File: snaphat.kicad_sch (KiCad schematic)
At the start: 140 parts, among them J1 Conn_01x08_S8B-PH-K-S(LF)(SN), J2 Conn_02x20_2214SM-40G-75-PCR, J3 Conn_01x02_B2B-PH-K-S(LF)(SN), J4 USB_C_USB4125-GF-A-0190, J5 Conn_01x03_MC34747, Q1 Q_BC817-25, Q2 Q_NTR4003NT1G, Q3 Q_NTR4003NT1G, SW1 SW_B3FS-1050, SW2 SW_B3FS-1050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

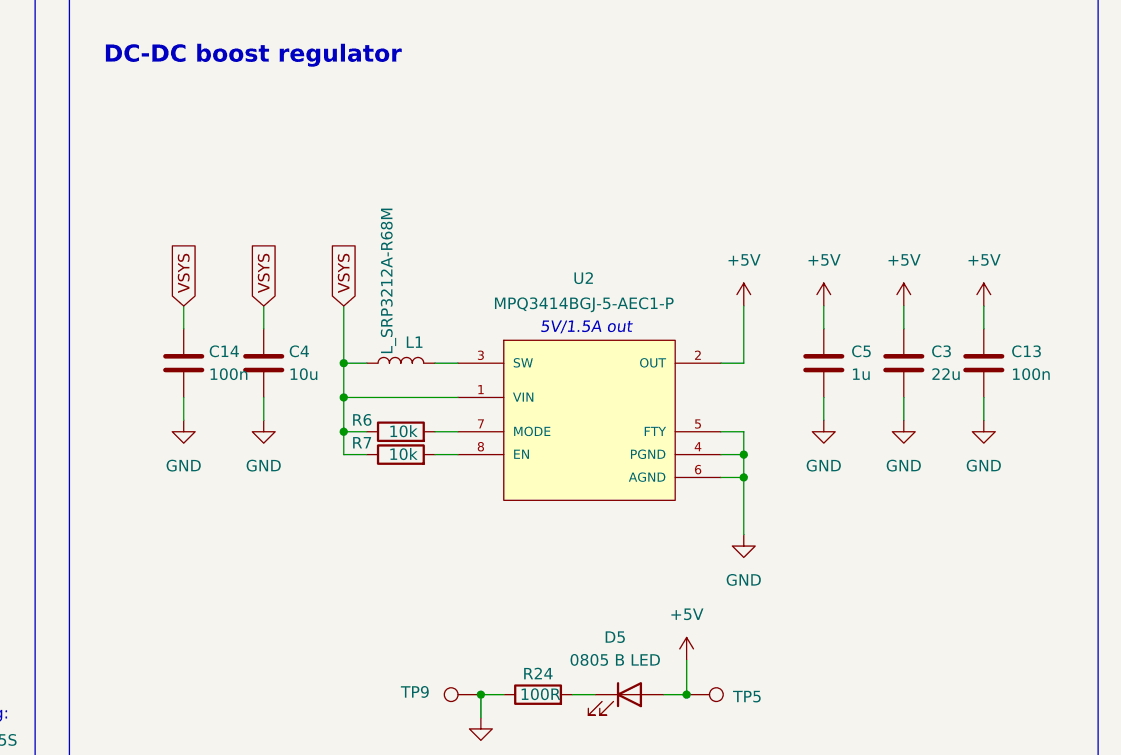
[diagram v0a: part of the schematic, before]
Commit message: Replace boost regulator with MIC2250-1YD5-TR
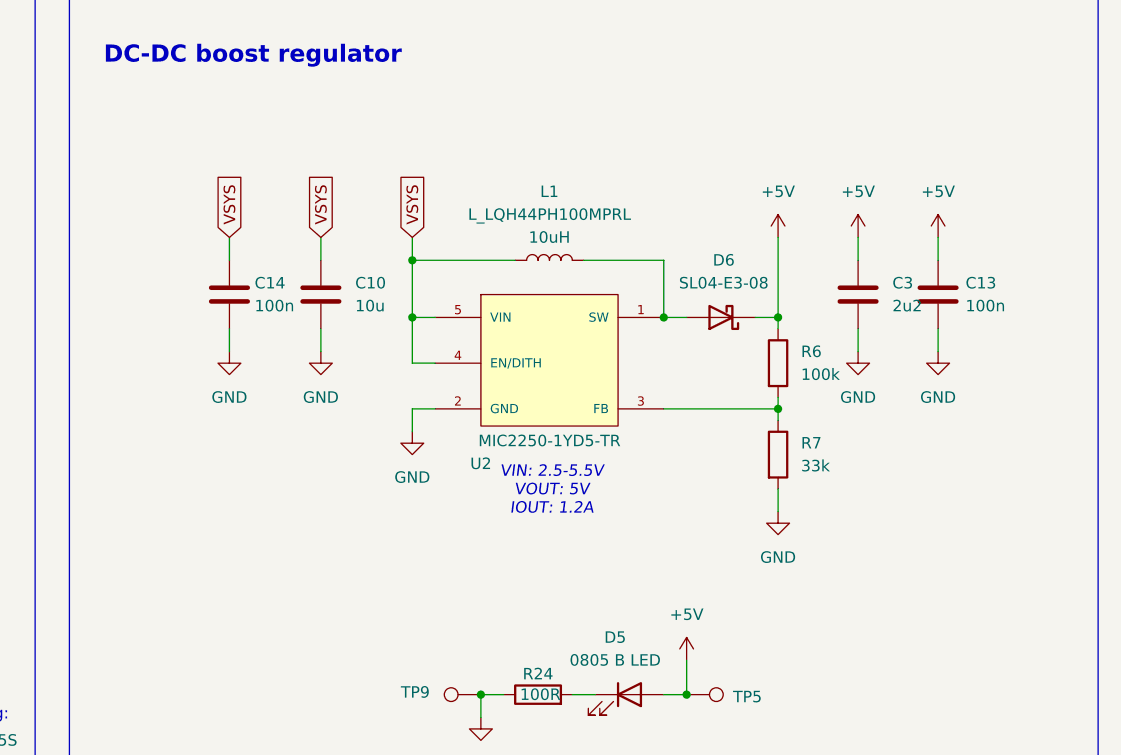
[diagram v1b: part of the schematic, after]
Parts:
- removed C3: 22u, library:C_0805_2012Metric, symbol library:C_22u_0805
- removed C4: 10u, library:C_0805_2012Metric, symbol library:C_10u_0805
- removed C5: 1u, library:C_0805_2012Metric, symbol library:C_1u_0805
- removed L1: L_SRP3212A-R68M, library:L_1210_3225Metric, symbol library:L_SRP3212A-R68M
- removed R6, R7: 10k, library:R_0402_1005Metric, symbol library:R_10k_0402
- removed U2: MPQ3414BGJ-5-AEC1-P, library:TSOT-23-8, symbol library:MPQ3414BGJ-5-AEC1-P
- added C10: 10u, library:C_0805_2012Metric, symbol library:C_10u_0805
- added C3: 2u2, library:C_0805_2012Metric, symbol library:C_2u2_0805
- added D6: SL04-E3-08, library:DO-219AB, symbol library:D_SL04-E3-08
- added L1: L_LQH44PH100MPRL, library:L_LPH44PH, symbol library:L_LQH44PH100MPRL
- added R6: 100k, library:R_0402_1005Metric, symbol library:R_100k_0402
- added R7: 33k, library:R_0402_1005Metric, symbol library:R_33k_0402
- added U2: MIC2250-1YD5-TR, library:TSOT-23-5, symbol library:MIC2250-1YD5-TR
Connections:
- net +5V: now also C3.1, D6.1 (K), R6.1
- net GND: now also C10.2, C3.2, R7.2, U2.2 (GND)
- net VSYS: now also C10.1, L1.1, U2.4 (EN/DITH), U2.5 (VIN)
- new net: D6.2 (A), L1.2, U2.1 (SW)
- new net: R6.2, R7.1, U2.3 (FB)
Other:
- note added: "VIN: 2.5-5.5V VOUT: 5V IOUT: 1.2A"
- note removed: "5V/1.5A out"
- moved on the sheet: C13, C14

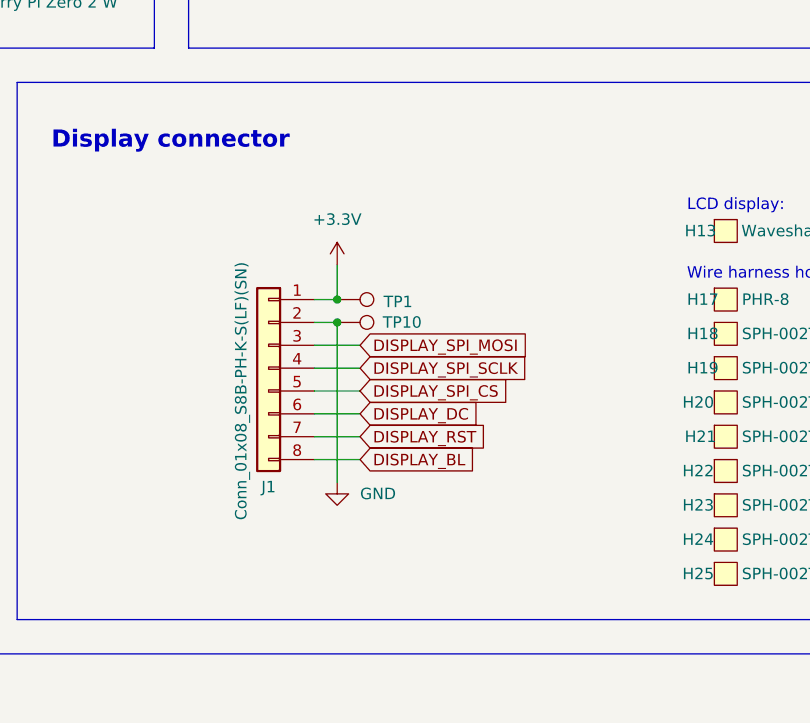
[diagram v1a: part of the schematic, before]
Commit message: Add display backlight pulldown
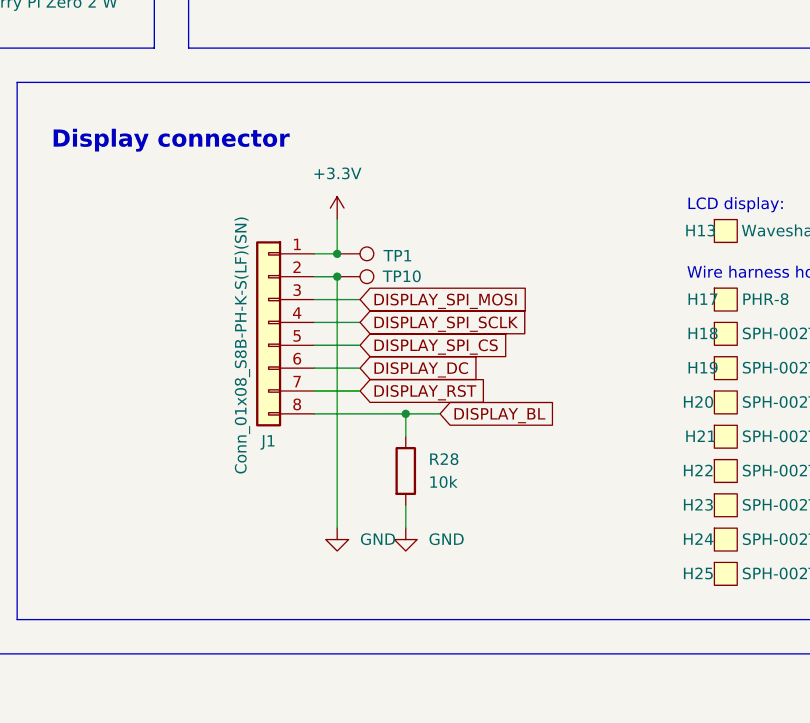
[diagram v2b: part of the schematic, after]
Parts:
- added R28: 10k, library:R_0402_1005Metric, symbol library:R_10k_0402
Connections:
- net DISPLAY_BL: now also R28.1
- net GND: now also R28.2
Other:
- moved on the sheet: J1, TP1, TP10

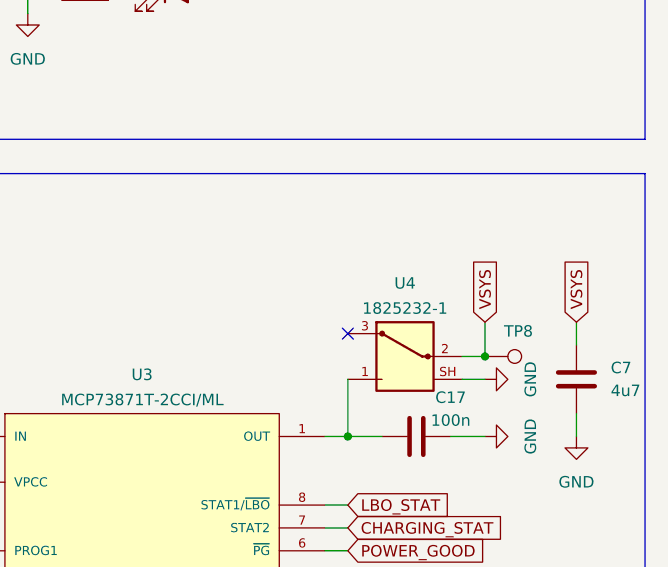
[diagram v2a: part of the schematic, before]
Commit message: Update slide switch reference to SW
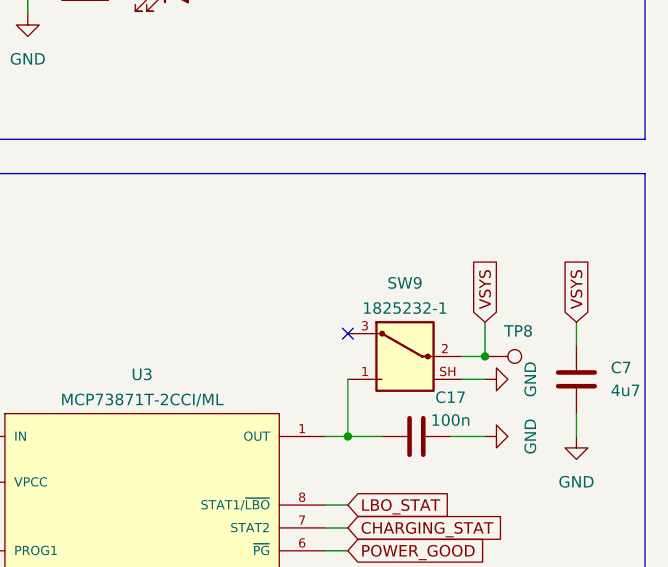
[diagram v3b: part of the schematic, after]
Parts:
- renumbered U4 to SW9
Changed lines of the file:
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@@
 		(on_board yes)
 		(dnp no)
-		(property "Reference" "U4"
+		(property "Reference" "SW9"
 			(at 377.19 126.492 0)
 			(effects
@@
 			(project ""
 				(path "/1b9269fa-3ac8-429a-ab83-4cc9a4203d51"
-					(reference "U4")
+					(reference "SW9")
 					(unit 1)
 				)

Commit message: Replace Q2 and Q3 with FDC6561AN
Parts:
- removed Q2, Q3: Q_NTR4003NT1G, library:SOT-23, symbol library:Q_NTR4003NT1G
- added Q4: Q_FDC6561AN, library:SSOT-6, symbol library:Q_FDC6561AN
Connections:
- net GND: now also Q4.2
- net GNDS: now also Q4.5
- net at U5.3 (CO): now also Q4.3
- net at U5.1 (DO): now also Q4.1
- new net: Q4.4, Q4.6

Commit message: Add USB OTG
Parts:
- removed J4: USB_C_USB4125-GF-A-0190, library:USB_C_Receptacle_GCT_USB4125-xx-x-0190_6P_TopMnt_Horizontal, symbol library:USB_C_USB4125-GF-A-0190
- added D7: SL04-E3-08, library:DO-219AB, symbol library:D_SL04-E3-08
- added D8: D_SMBJ5.0A, library:D_SMB, symbol library:SMBJ5.0A
- added H52: PHR-4, symbol library:PHR-4
- added H53, H54, H55, H56: SPH-002T-P0.5S, symbol library:SPH-002T-P0.5S
- added J4: USB_C_USB4930-00-A, symbol library:USB_C_USB4930-00-A
- added J6: Conn_01x04_B4B-PH-SM4-TB(LF)(SN), library:JST_B4B-PH-SM4-TB__SN_, symbol library:Conn_01x04_B4B-PH-SM4-TB(LF)(SN)
- added U4: TPD2EUSB30DRTR, library:Texas_DRT-3, symbol library:TPD2EUSB30DRTR
- Q4: footprint FDC6561AN:SSOT-6 -> library:SSOT-6
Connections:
- net GND: now also D8.1 (A1), J4.A1 (GND), J4.A12 (GND), J4.B1 (GND), J4.B12 (GND), J4.S1 (SHIELD), J6.4 (Pin_4), U4.3 (GND)
- net VBUS: now also D7.1 (K), J6.1 (Pin_1)
- net at R5.1: now also J4.A5 (CC1)
- net at R4.1: now also J4.B5 (CC2)
- new net: D7.2 (A), D8.2 (A2), J4.A4 (VBUS), J4.A9 (VBUS), J4.B4 (VBUS), J4.B9 (VBUS)
- new net USB_OTG_N: J4.A7 (D-), J4.B7 (D-), J6.3 (Pin_3), U4.2 (D-)
- new net USB_OTG_P: J4.A6 (D+), J4.B6 (D+), J6.2 (Pin_2), U4.1 (D+)
- no-connect marks 9 -> 11
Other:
- note added: "Raspberry Pi header and USB OTG"
- note removed: "Raspberry Pi header"
- moved on the sheet: C15, C16, C17, C18, C2, C21, C6, C7, C8, J2, R11, R15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

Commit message: Move power supply block to separate sheet, bringup fixes
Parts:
- removed C1, C12, C13, C14, C16, C17, C18, C21: 100n, library:C_0402_1005Metric, symbol library:C_100n_0402
- removed C10, C6: 10u, library:C_0805_2012Metric, symbol library:C_10u_0805
- removed C3: 2u2, library:C_0805_2012Metric, symbol library:C_2u2_0805
- removed C7, C8: 4u7, library:C_0805_2012Metric, symbol library:C_4u7_0805
- removed D2: 0805 G LED, library:LED_0805_2012Metric, symbol library:LED_G_MP008291
- removed D3: 0805 R LED, library:LED_0805_2012Metric, symbol library:LED_R_MP008293
- removed D4, D5: 0805 B LED, library:LED_0805_2012Metric, symbol library:LED_B_MP008292
- removed D6: SL04-E3-08, library:DO-219AB, symbol library:D_SL04-E3-08
- removed H15: 10304, library:Li-Pol_battery_8x30x40mm, symbol library:10304
- removed H48, H49, H53, H54, H55, H56: SPH-002T-P0.5S, symbol library:SPH-002T-P0.5S
- removed H50: PHR-2, symbol library:PHR-2
- removed H52: PHR-4, symbol library:PHR-4
- removed J6: Conn_01x04_B4B-PH-SM4-TB(LF)(SN), library:JST_B4B-PH-SM4-TB__SN_, symbol library:Conn_01x04_B4B-PH-SM4-TB(LF)(SN)
- removed L1: L_LQH44PH100MPRL, library:L_LPH44PH, symbol library:L_LQH44PH100MPRL
- removed Q4: Q_FDC6561AN, library:SSOT-6, symbol library:Q_FDC6561AN
- removed R10, R9: 150R, library:R_0402_1005Metric, symbol library:R_150R_0402
- removed R11, R13, R14, R15, R16, R18, R2, R28: 10k, library:R_0402_1005Metric, symbol library:R_10k_0402
- removed R12: 1k, library:R_0402_1005Metric, symbol library:R_1k_0402
- removed R17, R19: 0R, library:R_0402_1005Metric, symbol library:R_0R_0402
- removed R20: 2k7, library:R_0402_1005Metric, symbol library:R_2k7_0402
- removed R21: 330R, library:R_0805_2012Metric, symbol library:R_330R_0805
- removed R22, R23: 0R, library:R_0805_2012Metric, symbol library:R_0R_0805
- removed R24, R8: 100R, library:R_0402_1005Metric, symbol library:R_100R_0402
- removed R3: 0R01, library:R_2512_6332Metric, symbol library:R_0R01_2512
- removed R6: 100k, library:R_0402_1005Metric, symbol library:R_100k_0402
- removed R7: 33k, library:R_0402_1005Metric, symbol library:R_33k_0402
- removed SW9: 1825232-1, library:1825232-1, symbol library:1825232-1
- removed TP11, TP2, TP3, TP4, TP5, TP6, TP8, TP9: TestPoint, library:TestPoint_Pad_D1.5mm, symbol library:TestPoint
- removed U1: INA219BIDR, library:SOIC-8_3.9x4.9mm_P1.27mm, symbol library:INA219BIDR
- removed U2: MIC2250-1YD5-TR, library:TSOT-23-5, symbol library:MIC2250-1YD5-TR
- removed U3: MCP73871T-2CCI/ML, library:QFN-20-1EP_4x4mm_P0.5mm_EP2.7x2.7mm, symbol library:MCP73871T-2CCI_ML
- removed U5: AP9101CAK6-ABTRG1, library:SOT-26, symbol library:AP9101CAK6-ABTRG1
- added J10, J11, J12, J8, J9: P70-6000045R, library:HARWIN_P70-6000045R, symbol library:P70-6000045R
- added J6, J7: Conn_01x04_SFV4R-3STBE1HLF/C, library:AMPHENOL_SFV4R-3STBE1HLF, symbol library:Conn_01x04_SFV4R-3STBE1HLF/C
- added R28: 330R, library:R_0402_1005Metric, symbol library:R_330R_0402
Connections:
- net DISPLAY_BL: now also R28.1
- net GND: now also D8.2 (A2), R4.1, R5.1, J6.4 (Pin_4), R28.2; no longer D8.1 (A1), R4.2, R5.2
- net VBUS: now also J6.1 (Pin_1); no longer C15.2, C2.1
- net USBC_VBUS_IN: now reaches D7.2 (A), J4.A4 (VBUS), J4.A9 (VBUS), J4.B4 (VBUS), J4.B9 (VBUS)
- net USBC_VBUS_IN: now also C15.2, C2.1, D8.1 (A1); no longer D8.2 (A2)
- net at BZ1.2 (-), D1.2 (A): now also Q1.1 (C); no longer R27.1
- net OTG_EXT: now reaches R27.2
- net OTG_EXT: now also J12.1; no longer Q1.1 (C)
- net BATTERY_P: now reaches J3.1 (Pin_1)
- net at J4.A5 (CC1): now also R4.2; no longer R5.1
- net at J4.B5 (CC2): now also R5.2; no longer R4.1
- net GNDS renamed BATTERY_N
- net I2C_SCL renamed PM_SCL
- net I2C_SDA renamed PM_SDA
- net USB_OTG_N renamed USBC_DATA_N
- net USBC_DATA_N: now also J6.2 (Pin_2)
- net USB_OTG_P renamed USBC_DATA_P
- net USBC_DATA_P: now also J6.3 (Pin_3)
- new net GND_EXT: J11.1, J7.4 (Pin_4), R27.1
- new net USBC_EXT_DATA_N: J7.2 (Pin_2), J9.1
- new net USBC_EXT_DATA_P: J10.1, J7.3 (Pin_3)
- new net VBUS_EXT: J7.1 (Pin_1), J8.1
- no-connect marks 11 -> 10
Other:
- added sheet Power supply (power_supply.kicad_sch)
- note added: "FOOTPRINT WRONG"
- note added: "I2C address: 0x19"
- note added: "Replace with M2.5"
- note added: "This buzzer is kinda quiet"
- note added: "USB OTG extension board"
- note removed: "Battery charger"
- note removed: "Battery connector, protection and monitor"
- note removed: "DC-DC boost regulator"
- note removed: "I2C address: 0x18"
- note removed: "I2C address: 0x43"
- note removed: "Li-Po battery:"
- note removed: "Replace R27 with higher value to reduce buzzer volume"
- note removed: "VIN: 2.5-5.5V VOUT: 5V IOUT: 1.2A"
- moved on the sheet: BZ1, C15, C2, D1, D7, D8, J3, J4, R4, R5, TP7, U4

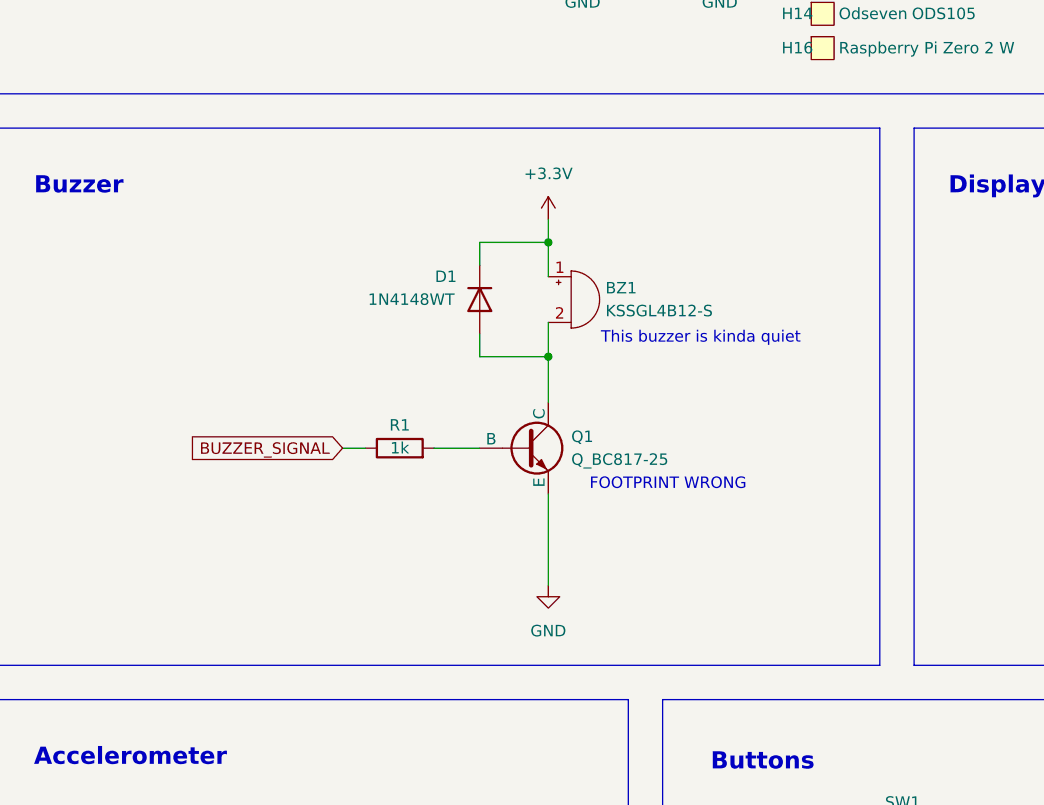
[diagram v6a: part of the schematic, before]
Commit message: Fix BC817-25 symbol (wrong pinout)
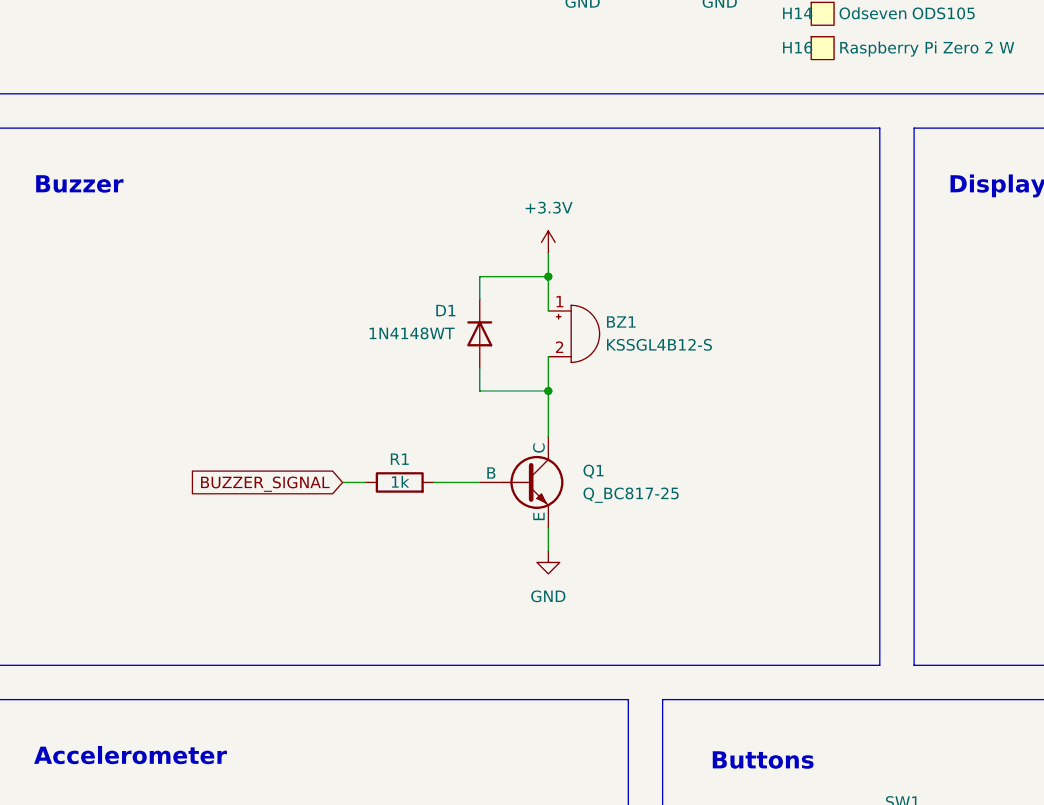
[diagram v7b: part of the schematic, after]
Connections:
- net GND: now also Q1.2 (E); no longer Q1.3 (E)
- net at R1.2: now also Q1.1 (B); no longer Q1.2 (B)
- net at BZ1.2 (-), D1.2 (A): now also Q1.3 (C); no longer Q1.1 (C)
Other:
- note removed: "This buzzer is kinda quiet"
- moved on the sheet: BZ1, D1, Q1, R1

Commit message: Update spacers
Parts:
- removed H18, H19, H20, H21, H22, H23, H24, H25: SPH-002T-P0.5S, symbol library:SPH-002T-P0.5S
- removed H26, H27, H28, H29: 9774030633R, library:Mounting_Wuerth_WA-SMSI-M1.6_H3mm_9774030633, symbol library:9774030633R
- removed H30, H31, H32: 970110151, library:970110151, symbol library:970110151
- removed H33, H34, H35, H36: M1.6x4, symbol library:M1.6x4
- removed H37, H38, H39: M2.5x5, symbol library:M2.5x5
- removed H51: M2.5 nut, symbol library:M2.5_nut
- added H18: PHR-8, symbol library:PHR-8
- added H19, H20, H21, H22, H23, H24, H25, H52: 01SPHSPH-26L-150, symbol library:01SPHSPH-26L-150
- added H26, H27, H28, H29: 9774030151R, library:Mounting_Wuerth_WA-SMSI-M2.5_H3mm_9774030151R, symbol library:9774030151R
- added H30, H31, H32, H33: 9774100151R, library:Mounting_Wuerth_WA-SMSI-M2.5_H10mm_9774100151R, symbol library:9774100151R
- added H34, H35, H36, H37: 9774020951R, library:Mounting_Wuerth_WA-SMST-2.7mm_H2mm_9774020951, symbol library:9774020951R
- added H53, H54, H55, H56: M2.5x5, symbol library:M2.5x5
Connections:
- net GND: now also H26.1, H27.1, H28.1, H29.1, H30.1, H31.1, H32.1, H33.1
- net GND_EXT: now also H34.1, H35.1, H36.1, H37.1
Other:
- note removed: "RPi standoffs:"
- note removed: "Replace with M2.5"
- moved on the sheet: H40, H41, H42, H43
